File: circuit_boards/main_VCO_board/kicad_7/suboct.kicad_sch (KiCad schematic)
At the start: 40 parts, among them U10 TL072, U11 TL072, U12 LM324, U9 4013

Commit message: Progress on circuit boards
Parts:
- C703, C705: value ? -> 100p
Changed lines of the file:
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@@
   (title_block
     (title "MICRO-OX Main VCO board")
-    (date "2023-03-27")
+    (date "2023-04-12")
     (rev "0")
     (comment 2 "creativecommons.org/licenses/by/4.0")
@@
   )
   (text_box "Saw connect trim.\n\nAdjust so that the slopes at the midpoint of the octave down sawtooth meet without a step."
-    (at 58.42 30.48 0) (size 24.13 13.97)
+    (at 58.42 27.94 0) (size 25.4 16.51)
     (stroke (width 0) (type default))
     (fill (type none))
@@
   )
   (text_box "Glitch trim\n\nAdjust for minimal glitch\nat the saw output."
-    (at 162.56 105.41 0) (size 19.05 11.43)
+    (at 162.56 105.41 0) (size 20.32 11.43)
     (stroke (width 0) (type default))
     (fill (type none))
@@
   )
   (text_box "The LM324 opamp is used here for its low slew rate, this helps to suppress some of the glitches from the wave mangling."
-    (at 248.92 68.58 0) (size 30.48 22.86)
+    (at 248.92 68.58 0) (size 33.02 25.4)
     (stroke (width 0) (type default))
     (fill (type none))
@@
     (effects (font (size 2 2)) (justify left bottom))
   )
-  (text "Downgoing SAW [-5, +5v]" (at 264.16 52.07 0)
+  (text "Downgoing SAW\n[-5, +5v]" (at 264.16 52.07 0)
     (effects (font (size 1.27 1.27)) (justify left bottom))
   )
   (text "SQUARE [0, +5v]\n\nRising edge coincident\nwith the falling edge\nof the input sawtooth"
-    (at 17.78 54.61 0)
+    (at 13.97 53.34 0)
     (effects (font (size 1.27 1.27)) (justify left bottom))
   )
@@
   (symbol (lib_id "Device:C") (at 215.9 33.02 270) (unit 1)
     (in_bom yes) (on_board yes) (dnp no) (fields_autoplaced)
-    (property "Reference" "C703" (at 215.9 25.4 90)
-      (effects (font (size 1.27 1.27)))
-    )
-    (property "Value" "?" (at 215.9 27.94 90)
+    (property "Reference" "C703" (at 215.9 26.67 90)
+      (effects (font (size 1.27 1.27)))
+    )
+    (property "Value" "100p" (at 215.9 29.21 90)
       (effects (font (size 1.27 1.27)))
     )
@@
   (symbol (lib_id "Device:C") (at 251.46 33.02 270) (unit 1)
     (in_bom yes) (on_board yes) (dnp no) (fields_autoplaced)
-    (property "Reference" "C705" (at 251.46 25.4 90)
-      (effects (font (size 1.27 1.27)))
-    )
-    (property "Value" "?" (at 251.46 27.94 90)
-      (effects (font (size 1.27 1.27)))
-    )
+    (property "Reference" "C705" (at 251.46 26.67 90)
+      (effects (font (size 1.27 1.27)))
+    )
+    (property "Value" "100p" (at 251.46 29.21 90)
+      (effects (font (size 1.27 1.27)))
+    )

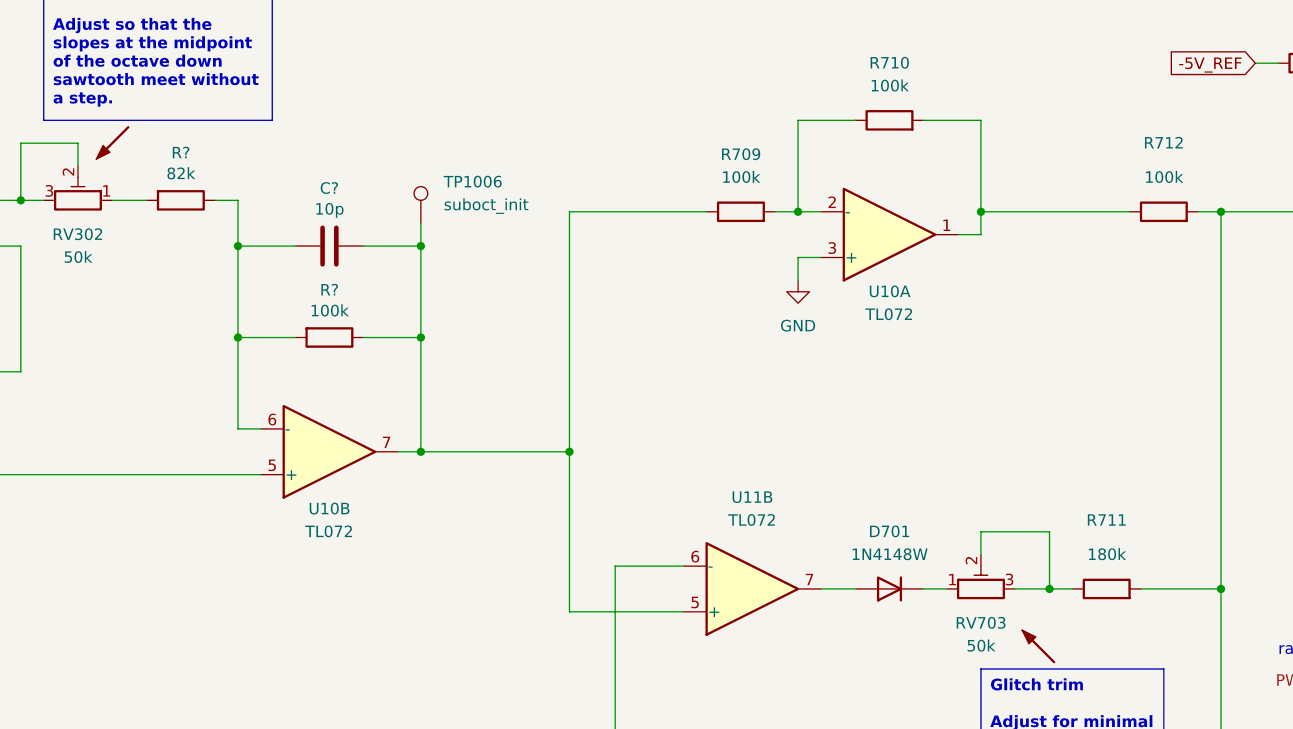
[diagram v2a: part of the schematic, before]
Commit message: Tweaks to VCO R values
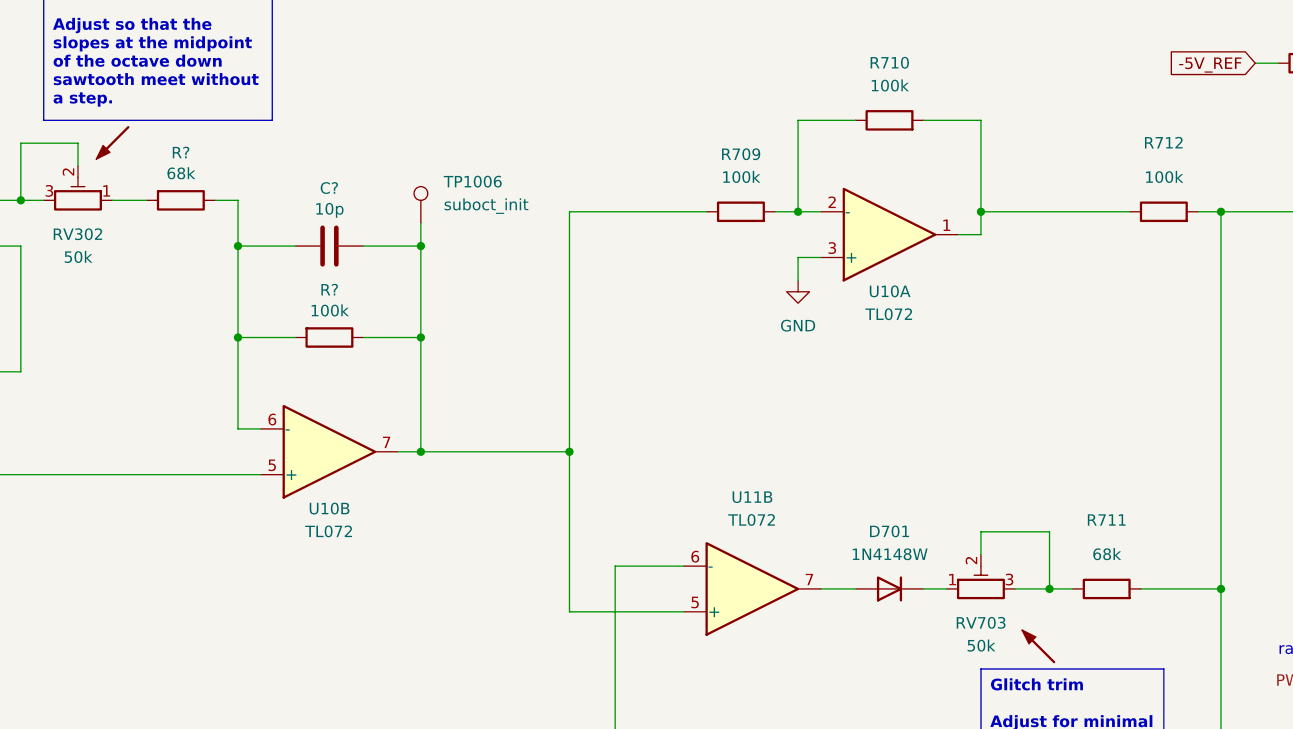
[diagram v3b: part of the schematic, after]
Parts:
- R711: value 180k -> 68k
- R?: value 82k -> 68k
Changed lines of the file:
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@@
       (effects (font (size 1.27 1.27)))
     )
-    (property "Value" "82k" (at 73.66 50.3936 90)
+    (property "Value" "68k" (at 73.66 50.3936 90)
       (effects (font (size 1.27 1.27)))
     )
@@
       (effects (font (size 1.27 1.27)))
     )
-    (property "Value" "180k" (at 176.53 92.71 90)
+    (property "Value" "68k" (at 176.53 92.71 90)
       (effects (font (size 1.27 1.27)))
     )

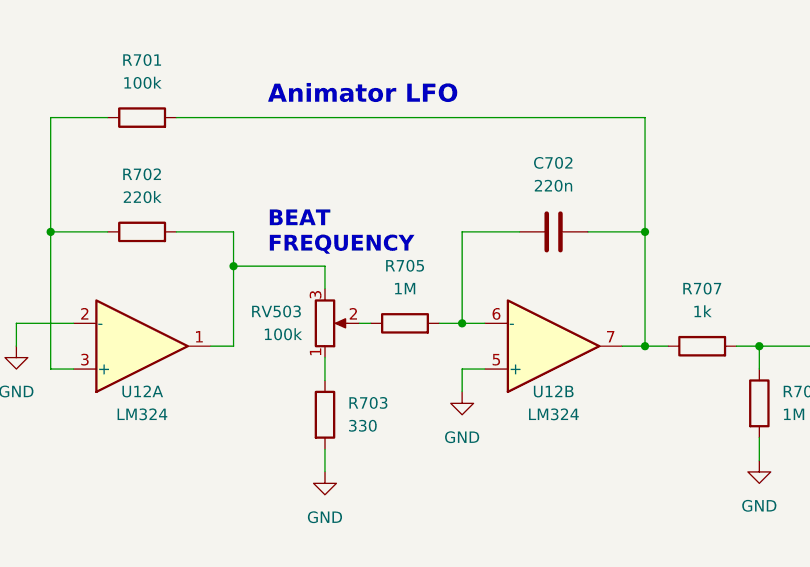
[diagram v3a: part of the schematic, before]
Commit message: Resistor tweaks while evaluating 1st build
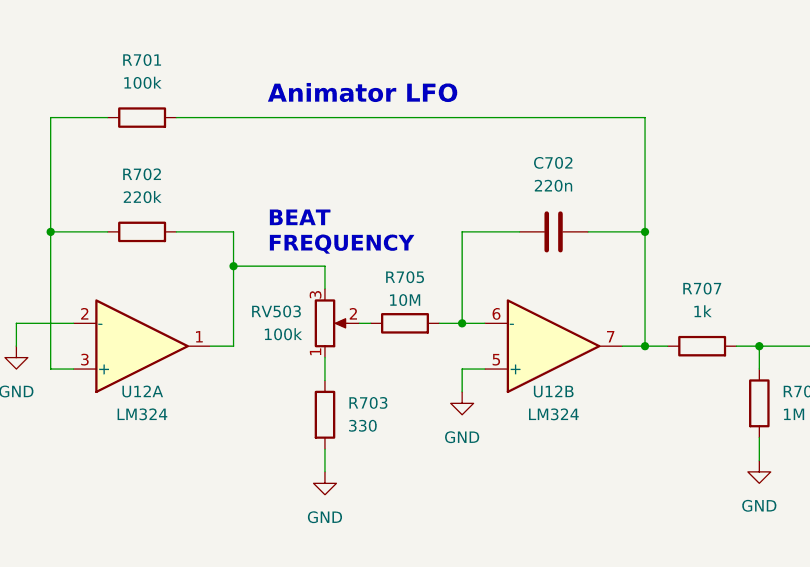
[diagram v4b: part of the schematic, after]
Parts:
- R705: value 1M -> 10M
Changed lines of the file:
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@@
   (symbol (lib_id "Device:R") (at 74.93 142.24 90) (unit 1)
     (in_bom yes) (on_board yes) (dnp no) (fields_autoplaced)
-    (property "Reference" "R705" (at 74.93 135.89 90)
+    (property "Reference" "R705" (at 74.93 137.16 90)
       (effects (font (size 1.27 1.27)))
     )
-    (property "Value" "1M" (at 74.93 138.43 90)
+    (property "Value" "10M" (at 74.93 139.7 90)
       (effects (font (size 1.27 1.27)))
     )

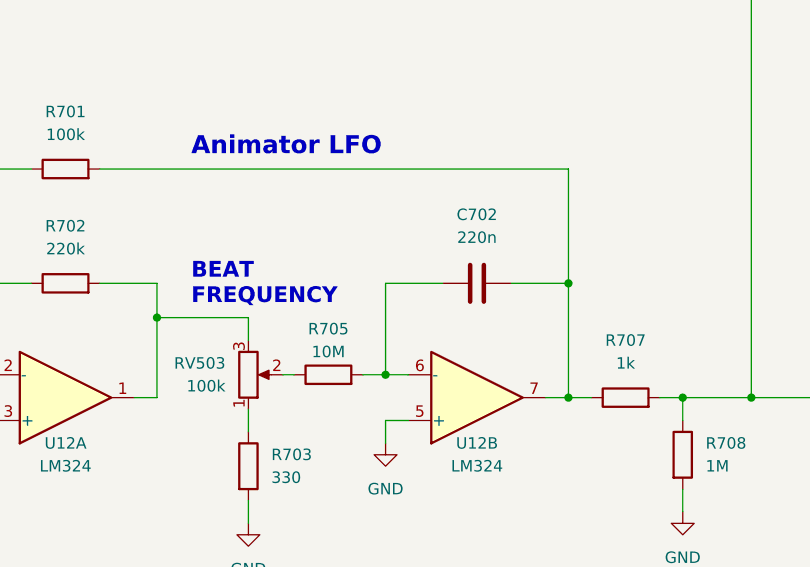
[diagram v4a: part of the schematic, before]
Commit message: Fix bug where animator LFO would rail out
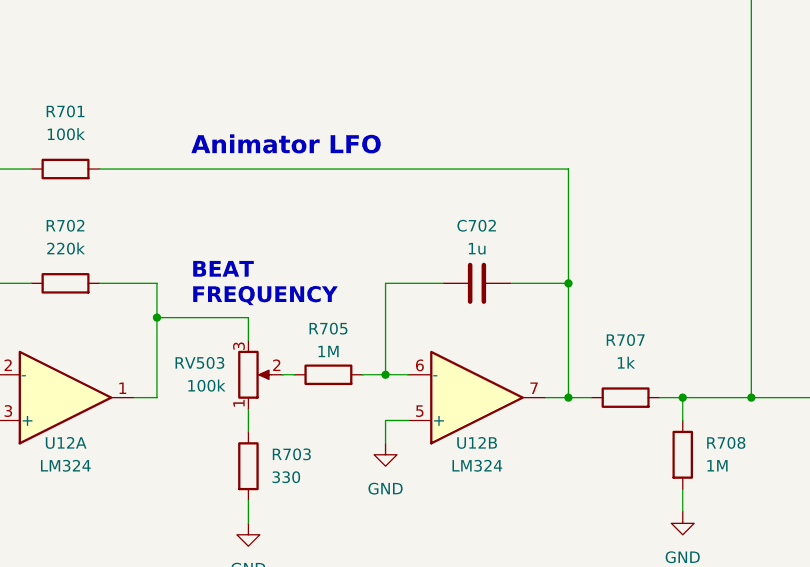
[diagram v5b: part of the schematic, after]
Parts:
- C702: value 220n -> 1u
- R705: value 10M -> 1M
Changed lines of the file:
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@@
   (symbol (lib_id "Device:C") (at 91.44 132.08 90) (unit 1)
     (in_bom yes) (on_board yes) (dnp no) (fields_autoplaced)
-    (property "Reference" "C702" (at 91.44 124.46 90)
+    (property "Reference" "C702" (at 91.44 125.73 90)
       (effects (font (size 1.27 1.27)))
     )
-    (property "Value" "220n" (at 91.44 127 90)
+    (property "Value" "1u" (at 91.44 128.27 90)
       (effects (font (size 1.27 1.27)))
     )
@@
       (effects (font (size 1.27 1.27)))
     )
-    (property "Value" "10M" (at 74.93 139.7 90)
+    (property "Value" "1M" (at 74.93 139.7 90)
       (effects (font (size 1.27 1.27)))
     )
